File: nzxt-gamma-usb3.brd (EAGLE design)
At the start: 94 x 21 mm, 5 parts, among them J1 SJ1-3545N, J2 SJ1-3545N, J3 GSB311131HR, J4 GSB311131HR

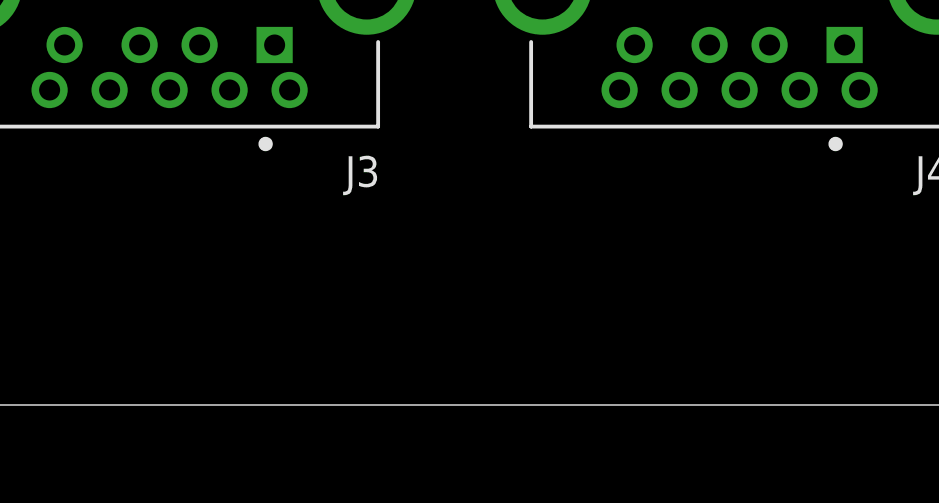
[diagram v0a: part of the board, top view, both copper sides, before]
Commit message: Added USB 3 IDC connector
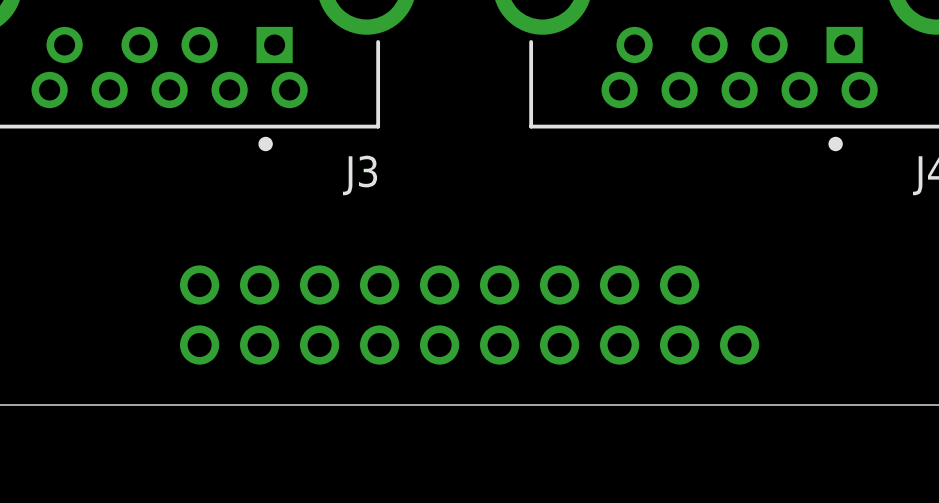
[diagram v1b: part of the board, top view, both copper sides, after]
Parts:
- added U$1: USB_IDC, usb3_idc:USB3_IDC
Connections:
- new net N$10: J3.3, U$1.11
- new net N$11: J3.5, U$1.18
- new net N$12: J3.6, U$1.17
- new net N$13: J3.8, U$1.15
- new net N$14: J3.9, U$1.14
- new net N$15: J4.2, U$1.8
- new net N$16: J4.3, U$1.9
- new net N$17: J4.5, U$1.2
- new net N$18: J4.6, U$1.3
- new net N$19: J4.8, U$1.5
- new net N$20: J4.9, U$1.6
- new net N$9: J3.2, U$1.12
- net +5V: now also U$1.1, U$1.19
- net GND: now also J3.4, J3.7, J4.4, J4.7, U$1.13, U$1.16, U$1.4, U$1.7
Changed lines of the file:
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@@
 </element>
 <element name="JP1" library="pinhead" library_urn="urn:adsk.eagle:library:325" package="2X05" package3d_urn="urn:adsk.eagle:package:22470/2" value="" x="77.47" y="5.08"/>
+<element name="U$1" library="usb3_idc" package="USB3_IDC" value="USB_IDC" x="46" y="2" rot="R180"/>
 </elements>
 <signals>
@@
 <contactref element="J3" pad="1"/>
 <contactref element="J4" pad="1"/>
+<contactref element="U$1" pad="19"/>
+<contactref element="U$1" pad="1"/>
 <wire x1="39.5" y1="12" x2="58.5" y2="12" width="0" layer="19" extent="1-1"/>
+<wire x1="53" y1="4" x2="39.5" y2="12" width="0" layer="19" extent="1-1"/>
+<wire x1="55" y1="2" x2="53" y2="4" width="0" layer="19" extent="1-1"/>
 </signal>
 <signal name="GND">
@@
 <contactref element="J4" pad="SH2"/>
 <contactref element="J4" pad="SH1"/>
-<wire x1="48.43" y1="14" x2="61.57" y2="14" width="0" layer="19" extent="1-1"/>
+<contactref element="U$1" pad="7"/>
+<contactref element="U$1" pad="4"/>
+<contactref element="U$1" pad="13"/>
+<contactref element="U$1" pad="16"/>
+<contactref element="J4" pad="7"/>
+<contactref element="J4" pad="4"/>
+<contactref element="J3" pad="7"/>
+<contactref element="J3" pad="4"/>
+<wire x1="55" y1="10.5" x2="61.57" y2="14" width="0" layer="19" extent="1-1"/>
+<wire x1="51.5" y1="12" x2="55" y2="10.5" width="0" layer="19" extent="1-1"/>
+<wire x1="48.43" y1="14" x2="51.5" y2="12" width="0" layer="19" extent="1-1"/>
 <wire x1="42.57" y1="14" x2="48.43" y2="14" width="0" layer="19" extent="1-1"/>
-<wire x1="29.43" y1="14" x2="42.57" y2="14" width="0" layer="19" extent="1-1"/>
+<wire x1="36" y1="10.5" x2="42.57" y2="14" width="0" layer="19" extent="1-1"/>
+<wire x1="32.5" y1="12" x2="36" y2="10.5" width="0" layer="19" extent="1-1"/>
+<wire x1="29.43" y1="14" x2="32.5" y2="12" width="0" layer="19" extent="1-1"/>
+<wire x1="41" y1="4" x2="36" y2="10.5" width="0" layer="19" extent="1-1"/>
+<wire x1="43" y1="2" x2="41" y2="4" width="0" layer="19" extent="1-1"/>
+<wire x1="47" y1="4" x2="43" y2="2" width="0" layer="19" extent="1-1"/>
+<wire x1="49" y1="2" x2="47" y2="4" width="0" layer="19" extent="1-1"/>
 </signal>
 <signal name="AGND">
@@
 <wire x1="84.455" y1="1.905" x2="90" y2="7.45" width="0.254" layer="16"/>
 </signal>
+<signal name="N$9">
+<contactref element="J3" pad="2"/>
+<contactref element="U$1" pad="12"/>
+<wire x1="39" y1="4" x2="37" y2="12" width="0" layer="19" extent="1-1"/>
+</signal>
+<signal name="N$10">
+<contactref element="U$1" pad="11"/>
+<contactref element="J3" pad="3"/>
+<wire x1="37" y1="4" x2="35" y2="12" width="0" layer="19" extent="1-1"/>
+</signal>
+<signal name="N$11">
+<contactref element="U$1" pad="18"/>
+<contactref element="J3" pad="5"/>
+<wire x1="51" y1="4" x2="32" y2="10.5" width="0" layer="19" extent="1-1"/>
+</signal>
+<signal name="N$12">
+<contactref element="J3" pad="6"/>
+<contactref element="U$1" pad="17"/>
+<wire x1="49" y1="4" x2="34" y2="10.5" width="0" layer="19" extent="1-1"/>
+</signal>
+<signal name="N$13">
+<contactref element="J3" pad="8"/>
+<contactref element="U$1" pad="15"/>
+<wire x1="45" y1="4" x2="38" y2="10.5" width="0" layer="19" extent="1-1"/>
+</signal>
+<signal name="N$14">
+<contactref element="J3" pad="9"/>
+<contactref element="U$1" pad="14"/>
+<wire x1="43" y1="4" x2="40" y2="10.5" width="0" layer="19" extent="1-1"/>
+</signal>
+<signal name="N$15">
+<contactref element="J4" pad="2"/>
+<contactref element="U$1" pad="8"/>
+<wire x1="41" y1="2" x2="56" y2="12" width="0" layer="19" extent="1-1"/>
+</signal>
+<signal name="N$16">
+<contactref element="U$1" pad="9"/>
+<contactref element="J4" pad="3"/>
+<wire x1="39" y1="2" x2="54" y2="12" width="0" layer="19" extent="1-1"/>
+</signal>
+<signal name="N$17">
+<contactref element="J4" pad="5"/>
+<contactref element="U$1" pad="2"/>
+<wire x1="53" y1="2" x2="51" y2="10.5" width="0" layer="19" extent="1-1"/>
+</signal>
+<signal name="N$18">
+<contactref element="U$1" pad="3"/>
+<contactref element="J4" pad="6"/>
+<wire x1="51" y1="2" x2="53" y2="10.5" width="0" layer="19" extent="1-1"/>
+</signal>
+<signal name="N$19">
+<contactref element="J4" pad="8"/>
+<contactref element="U$1" pad="5"/>
+<wire x1="47" y1="2" x2="57" y2="10.5" width="0" layer="19" extent="1-1"/>
+</signal>
+<signal name="N$20">
+<contactref element="U$1" pad="6"/>
+<contactref element="J4" pad="9"/>
+<wire x1="45" y1="2" x2="59" y2="10.5" width="0" layer="19" extent="1-1"/>
+</signal>
 </signals>

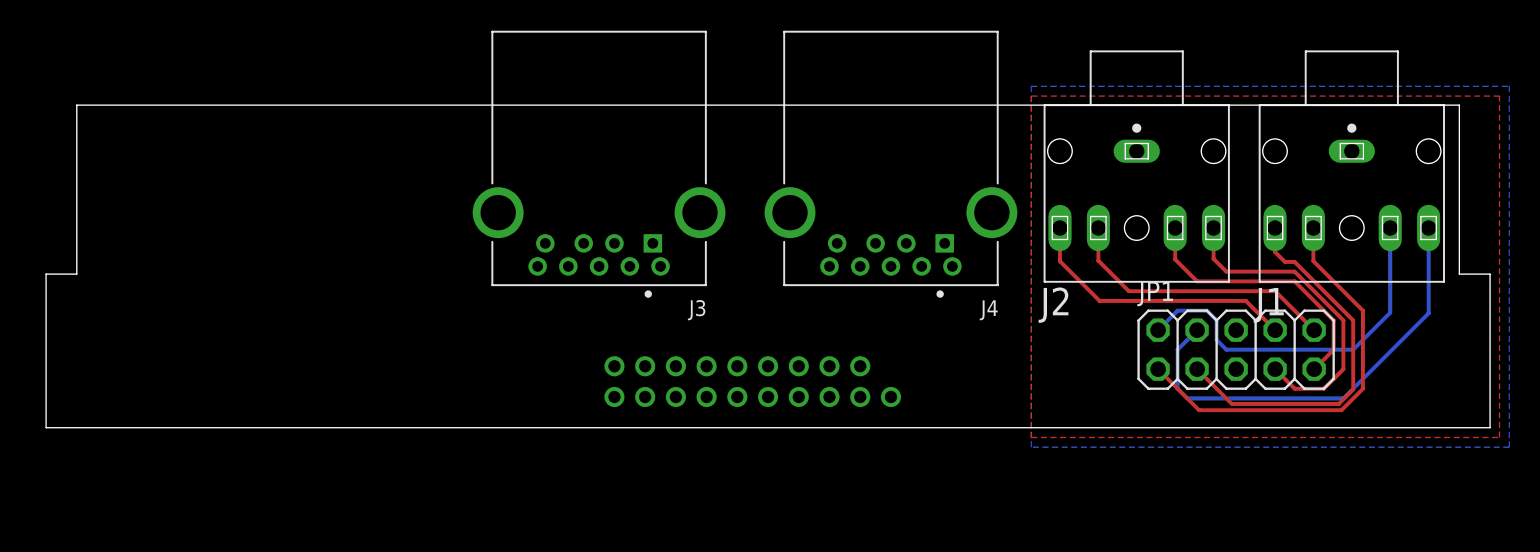
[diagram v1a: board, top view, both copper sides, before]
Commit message: Repositioned USB and eSATA ports to match casing better. started routing USB traces.
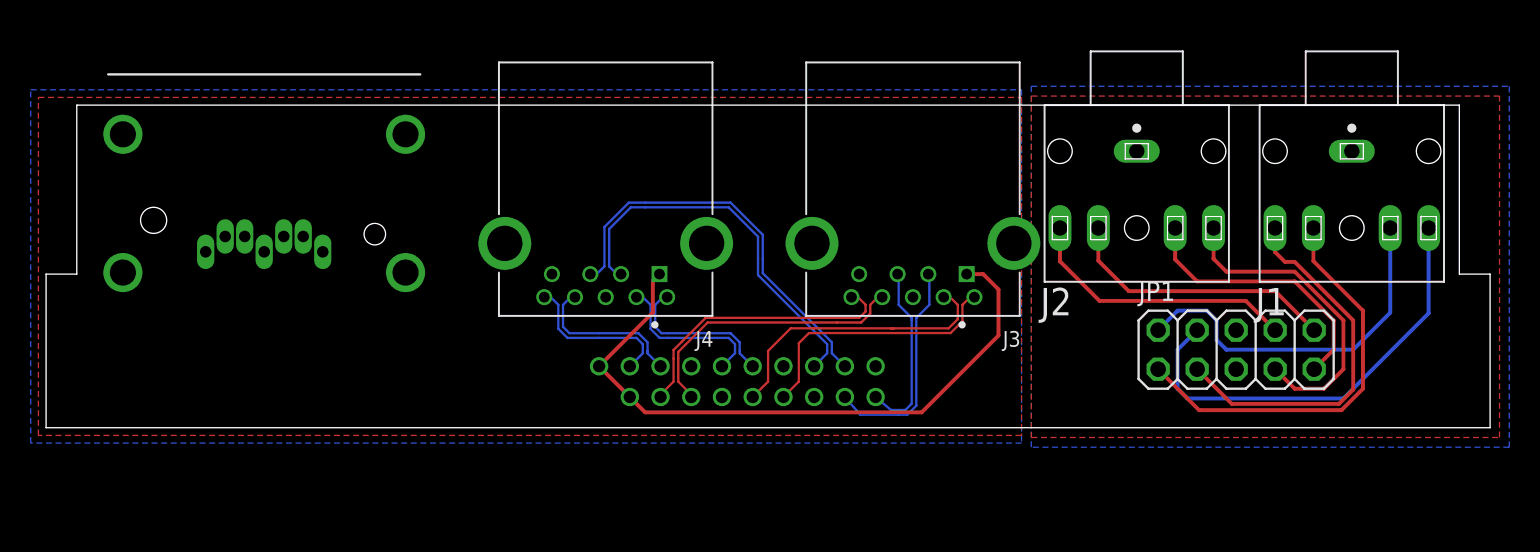
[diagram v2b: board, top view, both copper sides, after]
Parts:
- added U$2: G091208300LF, G091208300LF:G091208300LF
- moved J3 20.5 mm to (56.4, 10.0)
- moved J4 18.7 mm to (36.4, 10.0)
- moved U$1 2.24 mm to (45.0, 4.00), turned to 0 degrees
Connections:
- net N$10 renamed P2_D_P
- net N$11 renamed P2_SSRX_N
- net N$12 renamed P2_SSRX_P
- net N$13 renamed P2_SSTX_N
- net N$14 renamed P2_SSTX_P
- net N$15 renamed P1_D_N
- net N$16 renamed P1_D_P
- net N$17 renamed P1_SSRX_N
- net N$18 renamed P1_SSRX_P
- net N$19 renamed P1_SSTX_N
- net N$20 renamed P1_SSTX_P
- net N$9 renamed P2_D_N
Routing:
- net +5V: track 0.00 -> 42.4 mm
- net P1_D_P: track 0.00 -> 26.3 mm
- net P1_D_N: track 0.00 -> 25.1 mm
- net P2_SSTX_N: track 0.00 -> 18.9 mm
- net P2_SSRX_N: track 0.00 -> 18.5 mm
- net P2_SSRX_P: track 0.00 -> 18.4 mm
- net P2_SSTX_P: track 0.00 -> 17.2 mm
- net P2_D_N: track 0.00 -> 14.4 mm
- net P2_D_P: track 0.00 -> 11.6 mm
- net P1_SSTX_N: track 0.00 -> 10.4 mm
- net P1_SSRX_N: track 0.00 -> 10.4 mm
- net P1_SSTX_P: track 0.00 -> 10.3 mm
- net P1_SSRX_P: track 0.00 -> 10.3 mm
- added copper zone on layer 1, net GND
- added copper zone on layer 16, net GND

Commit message: Added sata connector. Length matched USB traces. Changed to managed libraries to generate 3D models.
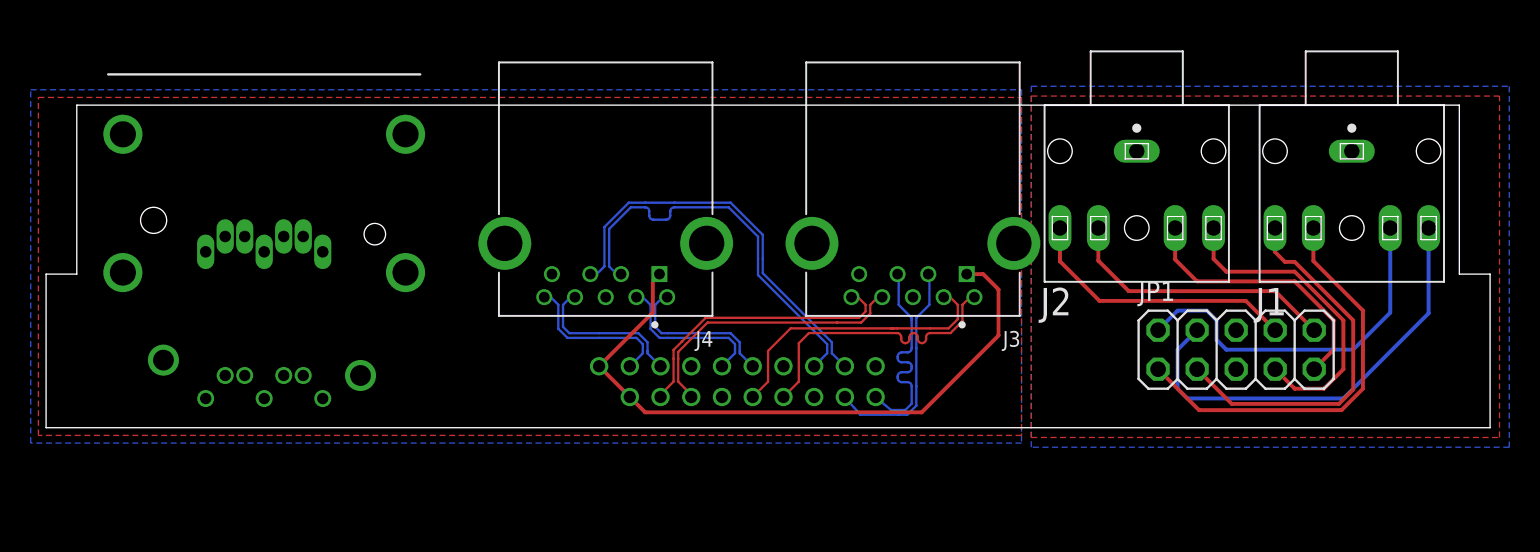
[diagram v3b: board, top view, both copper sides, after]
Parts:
- added U$3: 0678007001, dylans-parts:0678007001
- J1, J2: device SJ1-3545N:CUI_SJ1-3545N -> dylans-parts:CUI_SJ1-3545N
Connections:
- new net N$10: U$2.4, U$3.4
- new net N$11: U$2.7, U$3.7
- new net N$12: U$2.6, U$3.6
- new net N$13: U$2.5, U$3.5
- new net N$14: U$2.3, U$3.3
- new net N$15: U$2.2, U$3.2
- new net N$9: U$2.1, U$3.1
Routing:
- net P2_D_P: track 11.6 -> 14.0 mm
- net P2_SSTX_P: track 17.2 -> 18.6 mm
- net P1_D_N: track 25.1 -> 26.1 mm

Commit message: Updated components on board with better silkscreen
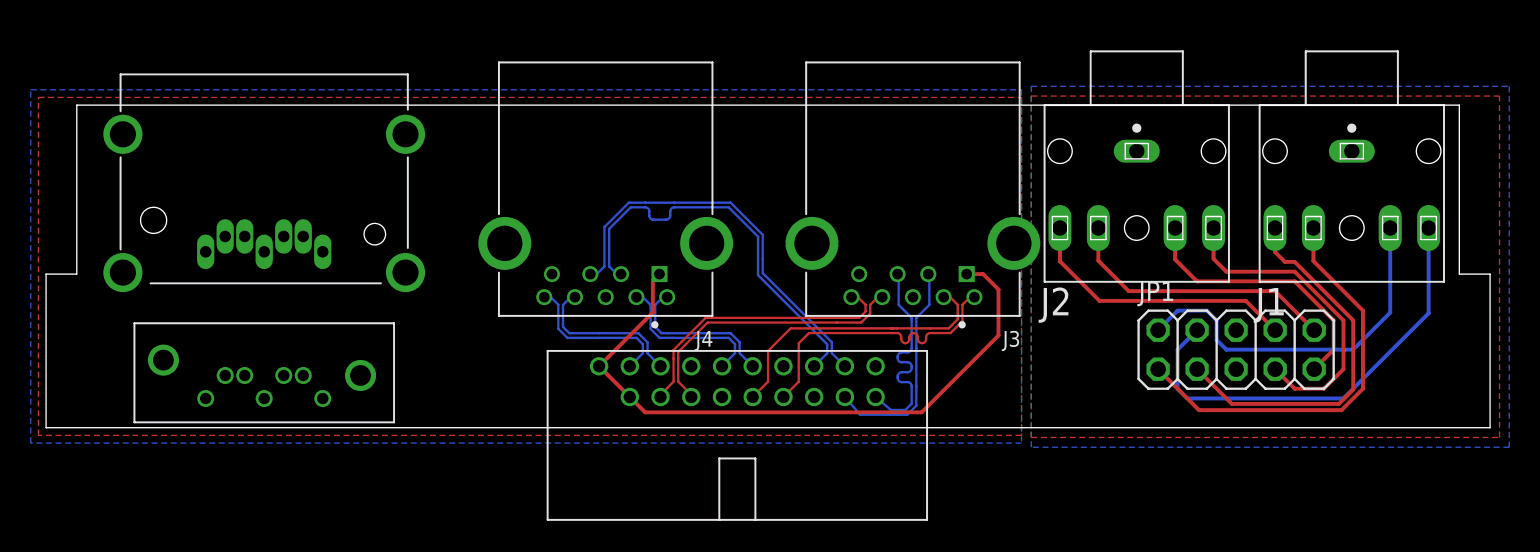
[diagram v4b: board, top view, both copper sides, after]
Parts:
- U$1: device usb3_idc:USB3_IDC -> dylans-parts:USB3_IDC
- U$2: device G091208300LF:G091208300LF -> dylans-parts:G091208300LF
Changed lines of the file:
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@@
 </layers>
 <board>
+<fusionsync huburn="a.cGVyc29uYWw6dWUyYTUxOTRm" projecturn="a.cGVyc29uYWw6dWUyYTUxOTRmIzIwMTgwNDAyMTI1NzMyMzA2" f3durn="urn:adsk.wipprod:dm.lineage:B2iLfHzZTAOEx9n-eYzeOw" pcbguid="ee7f4f14-b14e-46f0-b5cd-30ed6c26a326" lastpulledtime="" lastsyncedchangeguid="3d464b3e-d97d-efd3-59a3-118787275053"/>
 <plain>
 <wire x1="0" y1="0" x2="94" y2="0" width="0" layer="20"/>
@@
 <attribute name="VALUE" x="71.12" y="0.635" size="1.27" layer="27"/>
 </element>
-<element name="U$1" library="usb3_idc" package="USB3_IDC" value="USB_IDC" x="45" y="4" smashed="yes"/>
-<element name="U$2" library="G091208300LF" package="G091208300LF" value="G091208300LF" x="14.2" y="13" smashed="yes" rot="R180"/>
-<element name="U$3" library="dylans-parts" library_urn="urn:adsk.eagle:library:6331967" package="0678007001" package3d_urn="urn:adsk.eagle:package:6332269/1" value="0678007001" x="14.2" y="3.4" smashed="yes">
+<element name="U$1" library="dylans-parts" library_urn="urn:adsk.eagle:library:6331967" package="USB3_IDC" package3d_urn="urn:adsk.eagle:package:6332218/2" value="USB_IDC" x="45" y="4" smashed="yes"/>
+<element name="U$2" library="dylans-parts" library_urn="urn:adsk.eagle:library:6331967" package="G091208300LF" package3d_urn="urn:adsk.eagle:package:6332216/2" value="G091208300LF" x="14.2" y="13" smashed="yes" rot="R180"/>
+<element name="U$3" library="dylans-parts" library_urn="urn:adsk.eagle:library:6331967" package="0678007001" package3d_urn="urn:adsk.eagle:package:6332269/3" value="0678007001" x="14.2" y="3.4" smashed="yes">
 <attribute name="MF" value="Molex" x="14.2" y="3.4" size="1.778" layer="27" display="off"/>
 <attribute name="TYPE" value="SATA" x="14.2" y="3.4" size="1.778" layer="27" display="off"/>
@@
 </note>
 <note version="8.3" severity="warning">
+Since Version 8.3, EAGLE supports Fusion synchronisation.
+This feature will not be available in this version and saving
+the document will break the link to the Fusion PCB feature.
+</note>
+<note version="8.3" severity="warning">
